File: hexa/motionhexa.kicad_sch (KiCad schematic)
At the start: 2 parts, among them J1 Conn_01x13_Socket, J2 Conn_01x13_Socket

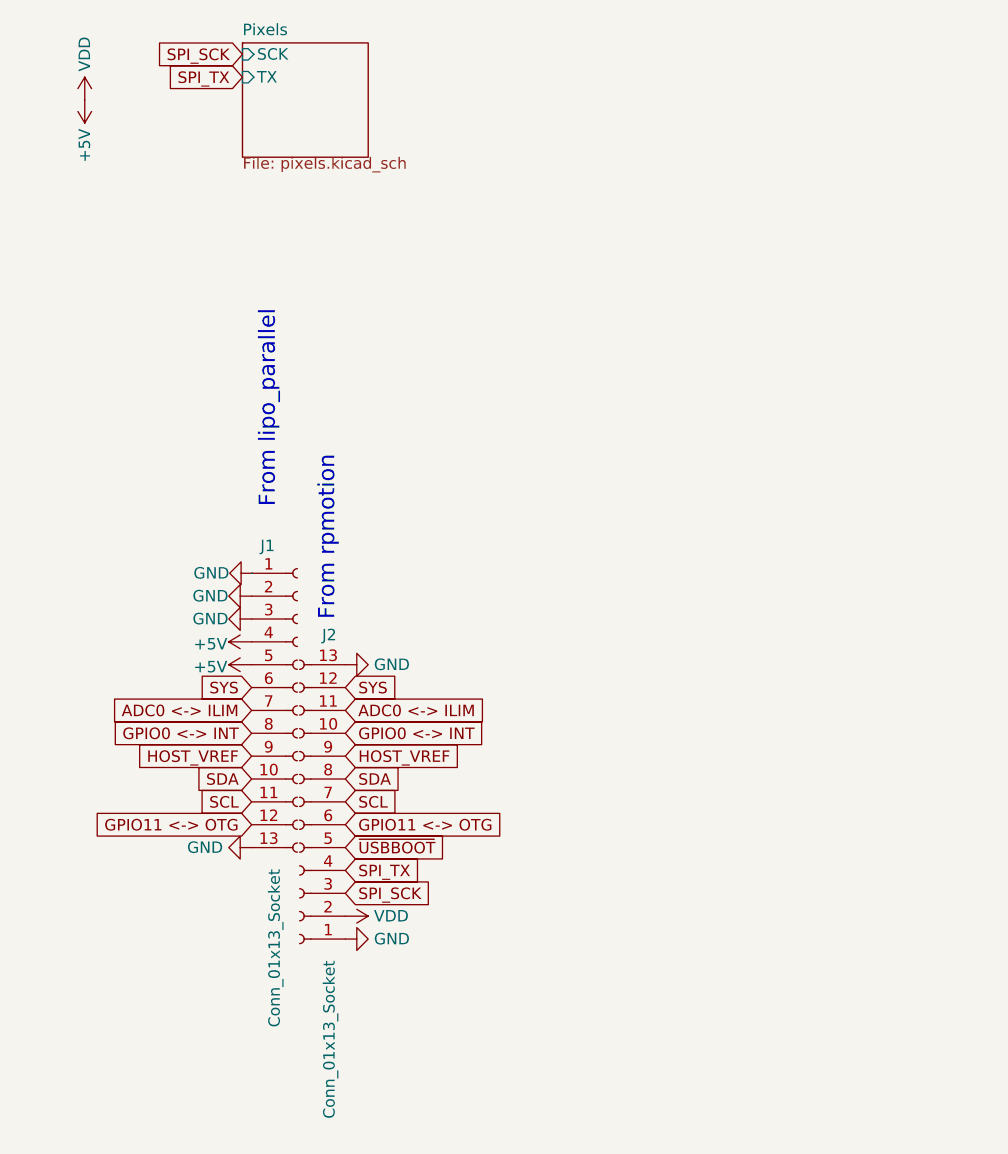
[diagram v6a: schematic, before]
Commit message: ERC fixes
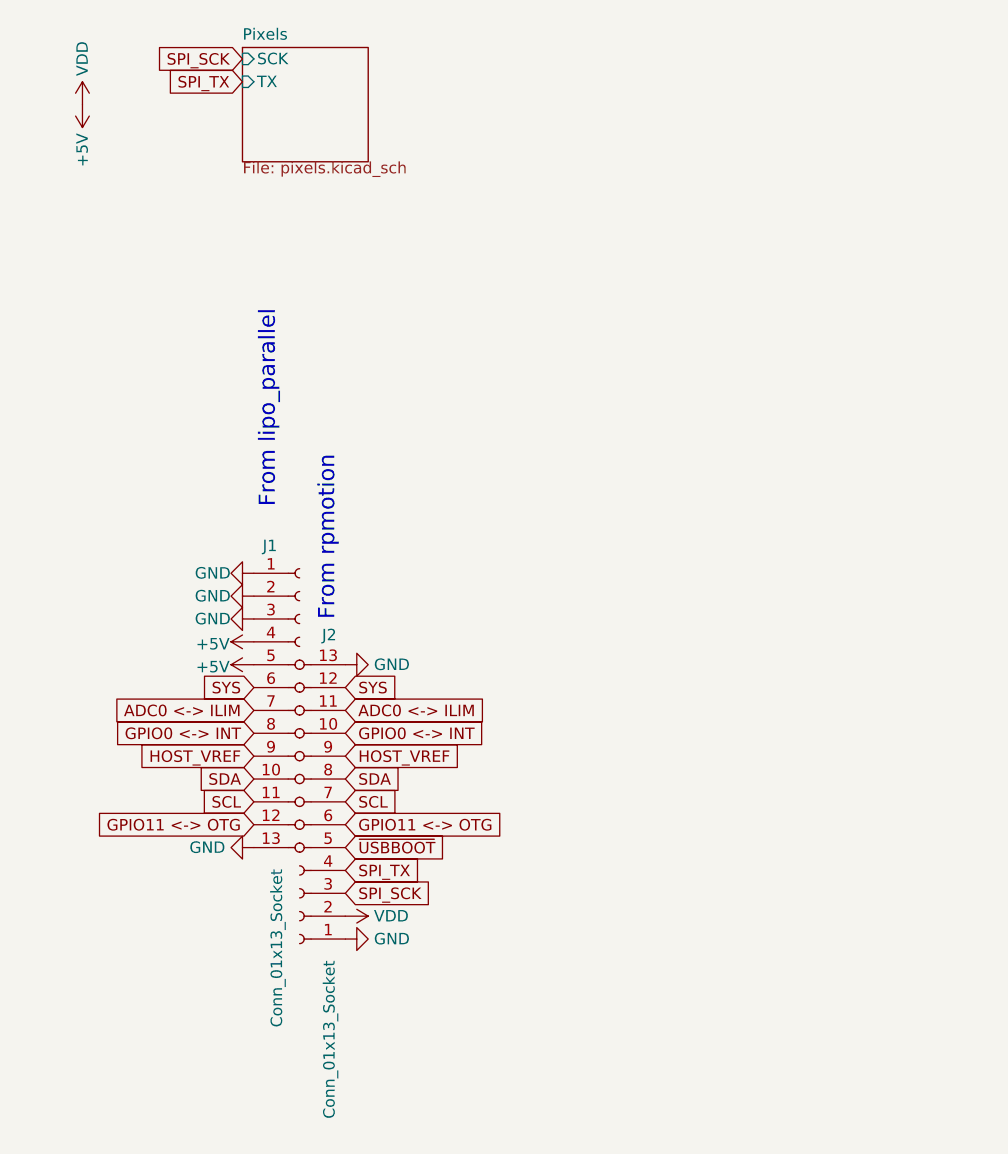
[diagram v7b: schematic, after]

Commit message: fix power routing so that VBUSes are connected across boards, +5v is correctly used for logic-level stepping, and a jumper from VBUS to +5V is available to power pixels if the lipo board is not being used; add some silkscreen labels; fix some DRC issues in footprints
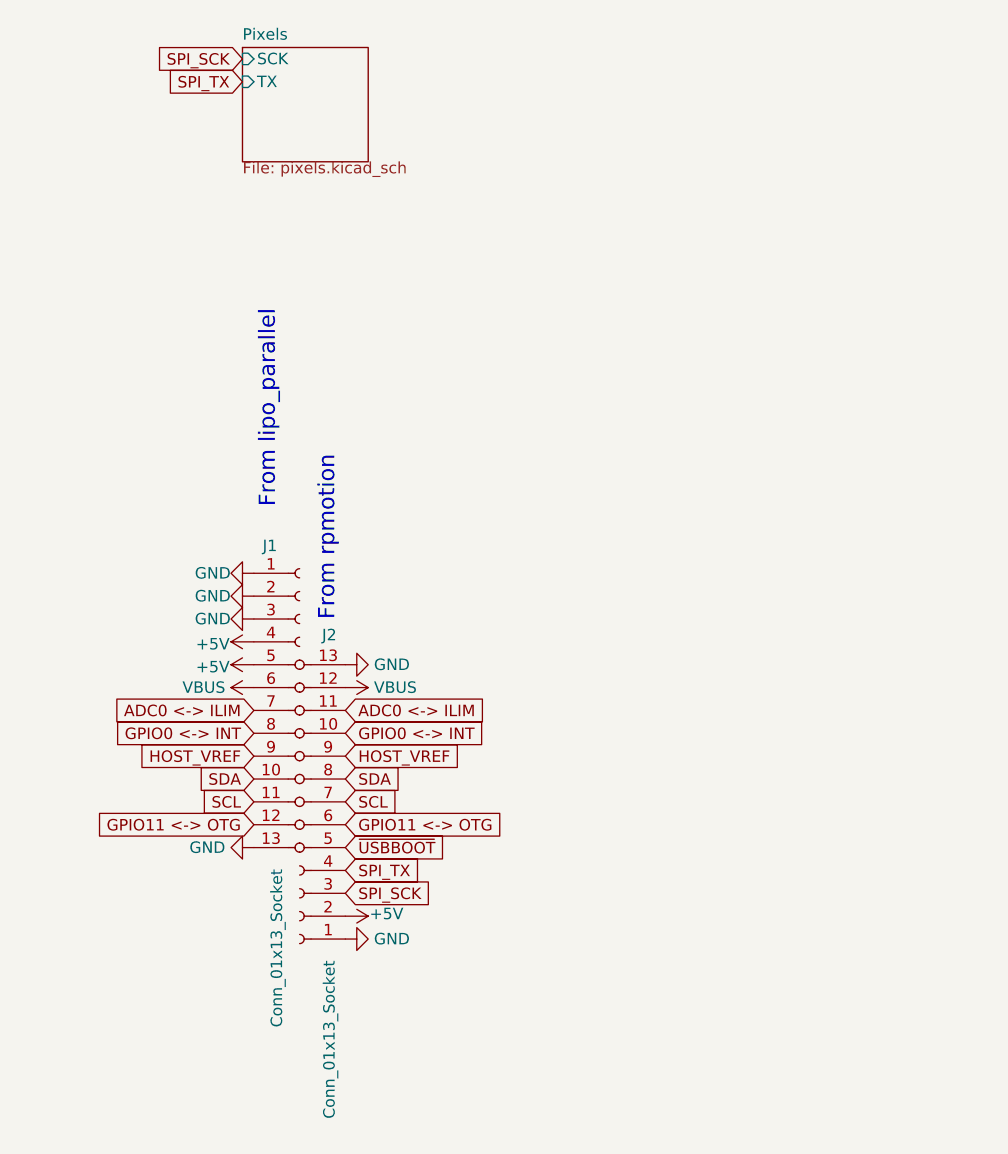
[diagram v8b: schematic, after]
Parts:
- J1, J2: now left out of the parts list
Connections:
- net SYS renamed VBUS
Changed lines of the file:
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@@
-    )
-  )
-  (global_label "SYS" (shape input) (at 116.84 95.25 0) (fields_autoplaced)
-    (effects (font (size 1.27 1.27)) (justify left))
-    (property "Intersheetrefs" "${INTERSHEET_REFS}" (at 123.3328 95.25 0)
-      (effects (font (size 1.27 1.27)) (justify left) hide)
-    )
-  )
-  (global_label "SYS" (shape input) (at 106.68 95.25 180) (fields_autoplaced)
-    (effects (font (size 1.27 1.27)) (justify right))
-    (property "Intersheetrefs" "${INTERSHEET_REFS}" (at 100.1872 95.25 0)
-      (effects (font (size 1.27 1.27)) (justify right) hide)
     )
   )
@@
     )
   )
-  (symbol (lib_id "power:VDD") (at 87.63 30.48 0) (unit 1)
-    (in_bom yes) (on_board yes) (dnp no) (fields_autoplaced)
-    (property "Reference" "#PWR03" (at 87.63 34.29 0)
-      (effects (font (size 1.27 1.27)) hide)
-    )
-    (property "Value" "VDD" (at 87.63 27.305 90)
-      (effects (font (size 1.27 1.27)) (justify left))
-    )
-    (property "Footprint" "" (at 87.63 30.48 0)
-      (effects (font (size 1.27 1.27)) hide)
-    )
-    (property "Datasheet" "" (at 87.63 30.48 0)
-      (effects (font (size 1.27 1.27)) hide)
-    )
-    (pin "1")
-    (instances
-      (project "motionhexa"
-        (path "/532d7ce0-7387-4a95-852a-321dca6ae013"
-          (reference "#PWR03") (unit 1)
-        )
-      )
-    )
-  )
   (symbol (lib_id "Connector:Conn_01x13_Socket") (at 111.76 97.79 0) (unit 1)
-    (in_bom yes) (on_board yes) (dnp no)
+    (in_bom no) (on_board yes) (dnp no)
     (property "Reference" "J1" (at 108.458 79.502 0)
       (effects (font (size 1.27 1.27)))
@@
     )
   )
-  (symbol (lib_id "power:+5V") (at 87.63 30.48 180) (unit 1)
-    (in_bom yes) (on_board yes) (dnp no) (fields_autoplaced)
-    (property "Reference" "#PWR04" (at 87.63 26.67 0)
-      (effects (font (size 1.27 1.27)) hide)
-    )
-    (property "Value" "+5V" (at 87.63 33.6549 90)
-      (effects (font (size 1.27 1.27)) (justify left))
-    )
-    (property "Footprint" "" (at 87.63 30.48 0)
-      (effects (font (size 1.27 1.27)) hide)
-    )
-    (property "Datasheet" "" (at 87.63 30.48 0)
-      (effects (font (size 1.27 1.27)) hide)
-    )
-    (pin "1")
-    (instances
-      (project "motionhexa"
-        (path "/532d7ce0-7387-4a95-852a-321dca6ae013"
-          (reference "#PWR04") (unit 1)
-        )
-      )
-    )
-  )
   (symbol (lib_id "power:GND") (at 106.68 82.55 270) (unit 1)
     (in_bom yes) (on_board yes) (dnp no)
@@
     )
   )
+  (symbol (lib_id "power:VBUS") (at 106.68 95.25 90) (unit 1)
+    (in_bom yes) (on_board yes) (dnp no) (fields_autoplaced)
+    (property "Reference" "#PWR010" (at 110.49 95.25 0)
+      (effects (font (size 1.27 1.27)) hide)
+    )
+    (property "Value" "VBUS" (at 103.505 95.25 90)
+      (effects (font (size 1.27 1.27)) (justify left))
+    )
+    (property "Footprint" "" (at 106.68 95.25 0)
+      (effects (font (size 1.27 1.27)) hide)
+    )
+    (property "Datasheet" "" (at 106.68 95.25 0)
+      (effects (font (size 1.27 1.27)) hide)
+    )
+    (pin "1")
+    (instances
+      (project "motionhexa"
+        (path "/532d7ce0-7387-4a95-852a-321dca6ae013"
+          (reference "#PWR010") (unit 1)
+        )
+      )
+    )
+  )
   (symbol (lib_id "power:GND") (at 116.84 123.19 90) (unit 1)
     (in_bom yes) (on_board yes) (dnp no) (fields_autoplaced)
@@
   )
   (symbol (lib_id "Connector:Conn_01x13_Socket") (at 111.76 107.95 180) (unit 1)
-    (in_bom yes) (on_board yes) (dnp no)
+    (in_bom no) (on_board yes) (dnp no)
     (property "Reference" "J2" (at 115.062 89.408 0)
       (effects (font (size 1.27 1.27)))
@@
     )
   )
-  (symbol (lib_id "power:VDD") (at 116.84 120.65 270) (unit 1)
-    (in_bom yes) (on_board yes) (dnp no) (fields_autoplaced)
+  (symbol (lib_id "power:+5V") (at 116.84 120.65 270) (unit 1)
+    (in_bom yes) (on_board yes) (dnp no)
     (property "Reference" "#PWR01" (at 113.03 120.65 0)
       (effects (font (size 1.27 1.27)) hide)
     )
-    (property "Value" "VDD" (at 120.015 120.65 90)
-      (effects (font (size 1.27 1.27)) (justify left))
+    (property "Value" "+5V" (at 121.412 120.396 90)
+      (effects (font (size 1.27 1.27)))
     )
     (property "Footprint" "" (at 116.84 120.65 0)
@@
         )
       )
+    )
+  )
+  (symbol (lib_id "power:VBUS") (at 116.84 95.25 270) (unit 1)
+    (in_bom yes) (on_board yes) (dnp no) (fields_autoplaced)
+    (property "Reference" "#PWR08" (at 113.03 95.25 0)
+      (effects (font (size 1.27 1.27)) hide)
+    )
+    (property "Value" "VBUS" (at 120.015 95.25 90)
+      (effects (font (size 1.27 1.27)) (justify left))
+    )
+    (property "Footprint" "" (at 116.84 95.25 0)
+      (effects (font (size 1.27 1.27)) hide)
+    )
+    (property "Datasheet" "" (at 116.84 95.25 0)
+      (effects (font (size 1.27 1.27)) hide)
+    )
+    (pin "1")
+    (instances
+      (project "motionhexa"
+        (path "/532d7ce0-7387-4a95-852a-321dca6ae013"
+          (reference "#PWR08") (unit 1)
+        )
+      )
